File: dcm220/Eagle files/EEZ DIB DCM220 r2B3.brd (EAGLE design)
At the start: 145 x 95 mm, 231 parts, among them IC1 Si8662AB-B-IS1, IC10 LT3763EFE#PBF, IC11 MC33274ADR2G, IC12 LT3763EFE#PBF, IC2 TPS54060DGQ, IC3 Si8641AB-B-IS1, IC4 M24C32-WMN6P, IC5 LP2985-33DBVR, IC6 TPD4E001DRLR, IC7 MAX5715BAUD+, IC8 STM32F373C8T6, IC9 MC33272ADR2G, J1 4907, J2 571-0500, J3 571-0100, J4 571-0500, J5 571-0100, Q1 IRFR7546TRPBF, Q2 IRFR7546TRPBF, Q3 2N7002, Q4 BSS84, Q5 IRFR7546TRPBF, Q6 IRFR7546TRPBF, Q7 2N7002, Q8 BSS84, X1 172648-0102, X2 77317-104-28LF, X3 22-23-2061, X4 DS1024-2*5R0, Y1 LF XTAL026392

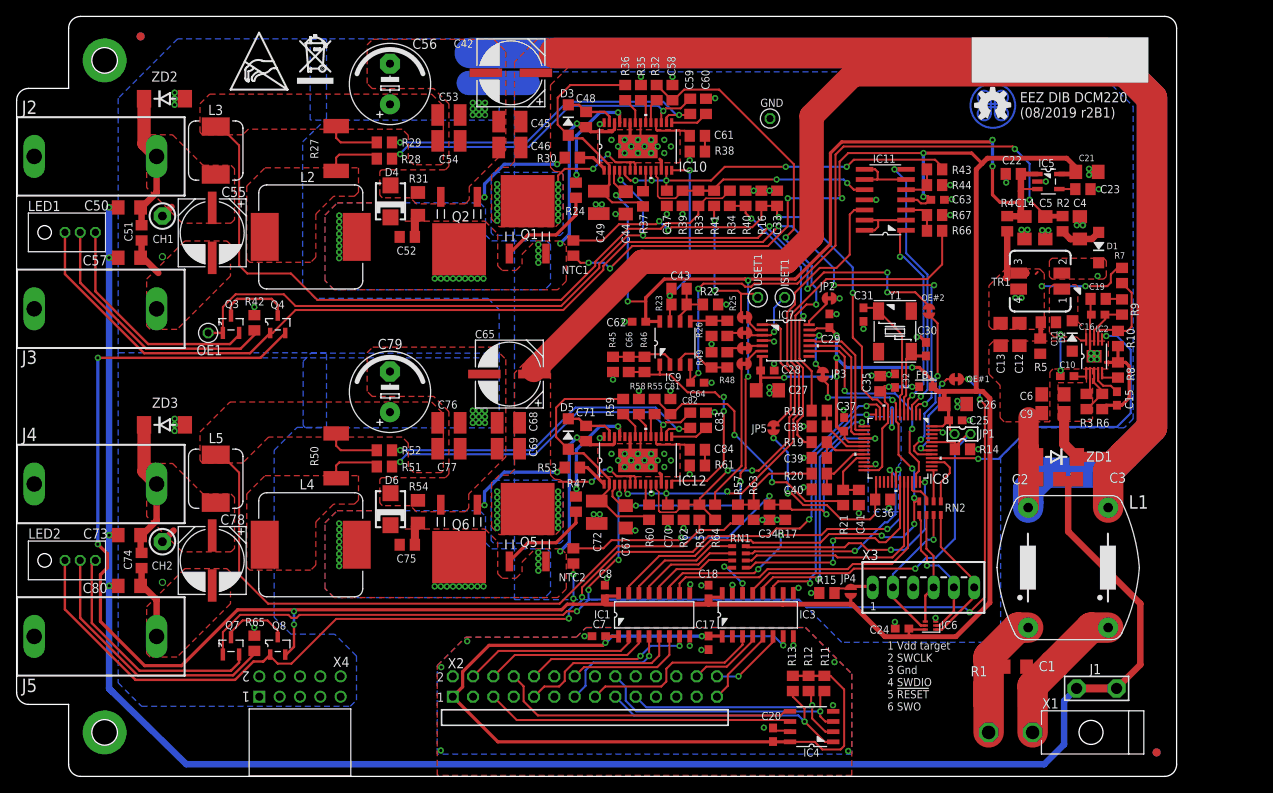
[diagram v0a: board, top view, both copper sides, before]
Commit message: #48, replaced DAC with PWM
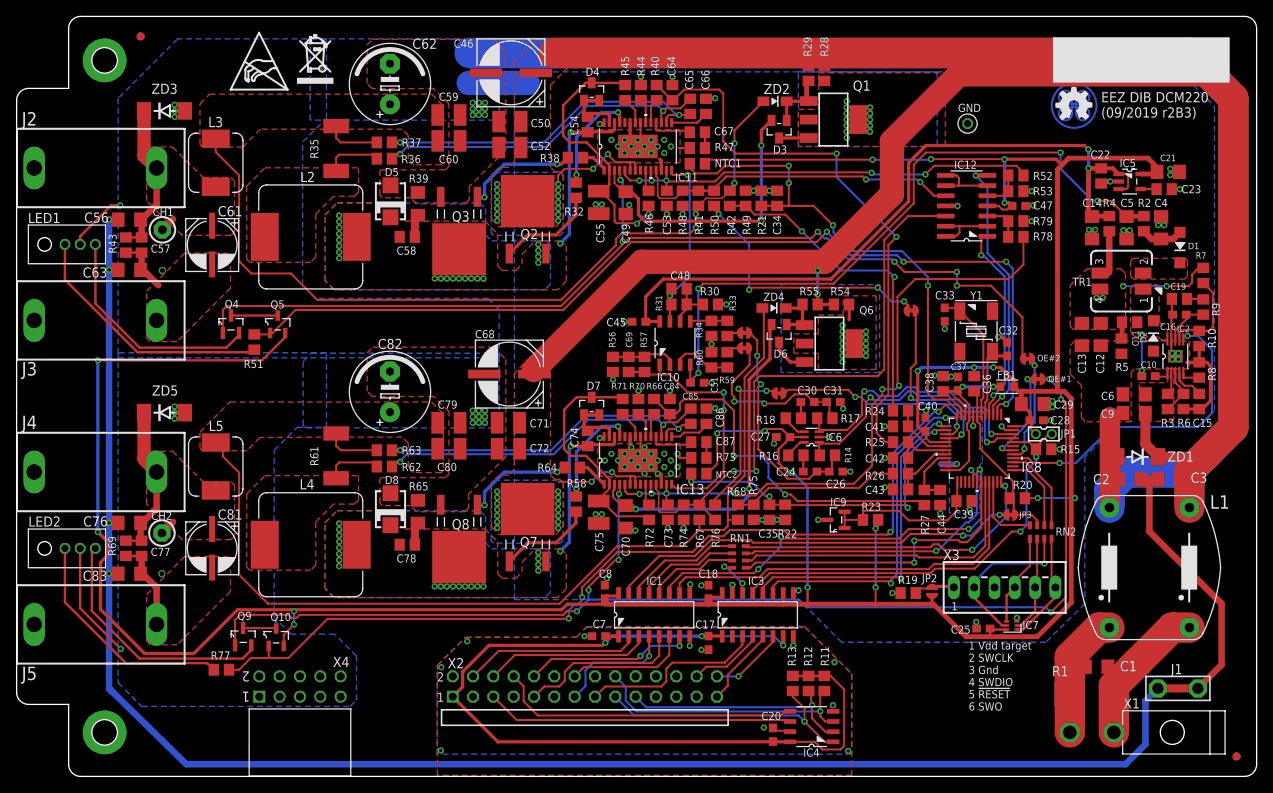
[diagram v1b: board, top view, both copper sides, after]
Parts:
- removed ISET1, OE1, USET1: (no value), EEZ_connectors:TEST-PIN_0.9MM
- removed JP4: JP2-CUT, EEZ_Lib1:JP2-CUT
- removed JP5: JP2-NOCUT, EEZ_Lib1:JP2-NOCUT
- added C85: 33n, rcl:C0805
- added C86: 10n, rcl:C0805
- added C87: 4n7, rcl:C0805
- added D7: BAW56L, EEZ_Lib1:SOT23
- added D8: N.C., EEZ_Lib1:SMA
- added IC13: LT3763EFE#PBF, EEZ_Lib1:LTC_05-08-1663-EB
- added Q10: BSS84, EEZ_Lib1:SOT95P237X112-3N
- added Q9: BSS205NH6327XTSA1, EEZ_Lib1:SOT103P240X110-3N
- added R68, R70: 86K6, rcl:R0805
- added R69: 3K3, rcl:R0805
- added R71, R72: 47K, rcl:R0805
- added R73: 30K, rcl:R0805
- added R74: 3K9, rcl:R0805
- added R75: 12K, rcl:R0805
- added R76: 3K6, rcl:R0805
- added R77: 120R, rcl:R0805
- added R78: 11K8, rcl:R0805
- added R79: 15K, rcl:R0805
- added ZD4: MM3Z9V1T1G, EEZ_Lib1:SOD323-W
- added ZD5: SMAJ51A, EEZ_Lib1:DO214AA
- C1, C2, C3: value 4n7/100V -> 10n/200V
- C15: value 100n -> 10n; device rcl:C0603 -> rcl:C0805
- C25: value 100n -> N.C.
- C26, C27: value 4u7 -> 100n; device rcl:C1206 -> rcl:C0603
- C29: value 100n -> 4u7; device rcl:C0603 -> rcl:C1206
- C30, C31: value 18p -> 100n
- C32: value 100n -> 4p7
- C33: value 10n -> 4p7; device rcl:C0805 -> rcl:C0603
- C35: value 1u -> 10n
- C36: value 100p -> 1n
- C38: value 3n3 -> 1u
- C39, C41: value 3n3 -> 4n7
- C40: value 3n3 -> 100n; device rcl:C0805 -> rcl:C0603
- C42: value EEEFK1V470P -> 4n7; device EEZ_Lib1:CAPAE830X1050N -> rcl:C0805
- C43: value 100p -> 4n7
- C44, C67: value 4u7 -> 4n7; device rcl:C1206 -> rcl:C0805
- C45: value 10u -> 100n; device rcl:C1210 -> rcl:C0603
- C46, C68: value 10u -> EEEFK1H470; device rcl:C1210 -> EEZ_Lib1:CAPAE830X1050N
- C47, C51: value 1u -> 100n; device rcl:C0805 -> rcl:C0603
- C48: value 220n -> 100p
- C49: value 22u -> 4u7; device rcl:C1210 -> rcl:C1206
- C50: value 10n/200V -> 10u; device rcl:C1206 -> rcl:C1210
- C52: value N.C. -> 10u; device rcl:C0805 -> rcl:C1210
- C53, C77: value 22u -> 1u; device rcl:C1210 -> rcl:C0805
- C54: value 22u -> 220n; device rcl:C1210 -> rcl:C0805
- C55: value EEEFK1V470P -> 22u; device EEZ_Lib1:CAPAE830X1050N -> rcl:C1210
- C56: value UVZ1E102MPD -> 10n/200V; device EEZ_Lib1:ECAP5/10.5 -> rcl:C1206
- C57, C73: value 10n/200V -> 1u; device rcl:C1206 -> rcl:C0805
- C58: value 470p -> N.C.
- C59: value 33n -> 22u; device rcl:C0805 -> rcl:C1210
- C60: value 10n -> 22u; device rcl:C0805 -> rcl:C1210
- C61: value 4n7 -> EEEFK1V470P; device rcl:C0805 -> EEZ_Lib1:CAPAE660X610N
- C62: value 100n -> UVZ1E102MPD; device rcl:C0603 -> EEZ_Lib1:ECAP5/10.5
- C63: value 100n -> 10n/200V; device rcl:C0603 -> rcl:C1206
- C64: value 100n -> 470p; device rcl:C0603 -> rcl:C0805
- C65: value EEEFK1V470P -> 33n; device EEZ_Lib1:CAPAE830X1050N -> rcl:C0805
- C66: value 100p -> 10n
- C69: value 10u -> 100p; device rcl:C1210 -> rcl:C0805
- C70: value 1u -> 4u7; device rcl:C0805 -> rcl:C1206
- C71: value 220n -> 10u; device rcl:C0805 -> rcl:C1210
- C72: value 22u -> 10u
- C74: value 1u -> 220n
- C75: value N.C. -> 22u; device rcl:C0805 -> rcl:C1210
- C76: value 22u -> 10n/200V; device rcl:C1210 -> rcl:C1206
- C78: value EEEFK1V470P -> N.C.; device EEZ_Lib1:CAPAE830X1050N -> rcl:C0805
- C79: value UVZ1E102MPD -> 22u; device EEZ_Lib1:ECAP5/10.5 -> rcl:C1210
- C80: value 10n/200V -> 22u; device rcl:C1206 -> rcl:C1210
- C81: value 470p -> EEEFK1V470P; device rcl:C0805 -> EEZ_Lib1:CAPAE660X610N
- C82: value 33n -> UVZ1E102MPD; device rcl:C0805 -> EEZ_Lib1:ECAP5/10.5
- C83: value 10n -> 10n/200V; device rcl:C0805 -> rcl:C1206
- C84: value 4n7 -> 470p
- D3: value SKL16 -> BAW56L; device EEZ_Lib1:SOD123 -> EEZ_Lib1:SOT23
- D4, D6: value N.C. -> BAW56L; device EEZ_Lib1:SMA -> EEZ_Lib1:SOT23
- D5: value SKL16 -> N.C.; device EEZ_Lib1:SOD123 -> EEZ_Lib1:SMA
- IC10: value LT3763EFE#PBF -> MC33272ADR2G; device EEZ_Lib1:LTC_05-08-1663-EB -> EEZ_Lib1:SOIC127P600X173-8N
- IC11: value MC33274ADR2G -> LT3763EFE#PBF; device EEZ_Lib1:SOIC127P600X175-14N -> EEZ_Lib1:LTC_05-08-1663-EB
- IC12: value LT3763EFE#PBF -> MC33274ADR2G; device EEZ_Lib1:LTC_05-08-1663-EB -> EEZ_Lib1:SOIC127P600X175-14N
- IC6: value TPD4E001DRLR -> 74HC2G04GW,125; device EEZ_Lib1:DRL6 -> EEZ_Lib1:SOT65P210X110-6N
- IC7: value MAX5715BAUD+ -> N.C.; device EEZ_Lib1:21-0066J_14 -> EEZ_Lib1:DRL6
- IC9: value MC33272ADR2G -> TL431B; device EEZ_Lib1:SOIC127P600X173-8N -> EEZ_Lib1:SOT103P240X110-3N
- JP2: value JP2-NOCUT -> JP2-CUT; device EEZ_Lib1:JP2-NOCUT -> EEZ_Lib1:JP2-CUT
- Q1, Q6: value IRFR7546TRPBF -> BSP716NH6327XTSA1; device EEZ_Lib1:TO229P990X239-3N -> transistor-power:SOT223
- Q2: value IRFR7546TRPBF -> NTD5867NLT4G
- Q3, Q7: value 2N7002 -> NTD5867NLT4G; device EEZ_Lib1:SOT103P240X110-3N -> EEZ_Lib1:TO229P990X239-3N
- Q4: value BSS84 -> BSS205NH6327XTSA1; device EEZ_Lib1:SOT95P237X112-3N -> EEZ_Lib1:SOT103P240X110-3N
- Q5: value IRFR7546TRPBF -> BSS84; device EEZ_Lib1:TO229P990X239-3N -> EEZ_Lib1:SOT95P237X112-3N
- Q8: value BSS84 -> NTD5867NLT4G; device EEZ_Lib1:SOT95P237X112-3N -> EEZ_Lib1:TO229P990X239-3N
- R1: value 4K7/2W -> N.C.
- R16, R17: value 3K3 -> 10K
- R18, R20: value 1K -> 10K
- R19: value 1K -> N.C.
- R21: value 1K -> 3K3
- R22: value 20K -> 3K3
- R23: value 12K -> 120R
- R24: value 0R -> 2K2
- R25: value 20K -> 2K2
- R26, R40: value 12K -> 2K2
- R27: value R012/2W -> 2K2; device EEZ_Lib1:R_2512-4WIRE -> rcl:R0805
- R29: value 10R -> 330K
- R30: value 0R -> 20K
- R31: value N.C. -> 12K; device rcl:R1206 -> rcl:R0805
- R32: value 2K2 -> 0R
- R33, R56: value 30K -> 20K
- R34, R57: value 86K6 -> 12K
- R35: value 86K6 -> R012/2W; device rcl:R0805 -> EEZ_Lib1:R_2512-4WIRE
- R36, R37: value 47K -> 10R
- R38: value 30K -> 0R
- R39: value 3K9 -> N.C.; device rcl:R0805 -> rcl:R1206
- R41: value 3K6 -> 30K
- R42: value 120R -> 86K6
- R43: value 11K8 -> 3K3
- R44: value 15K -> 86K6
- R45: value 20K -> 47K
- R46: value 12K -> 47K
- R47: value 0R -> 30K
- R48: value 20K -> 3K9
- R50: value R012/2W -> 3K6; device EEZ_Lib1:R_2512-4WIRE -> rcl:R0805
- R51: value 10R -> 120R
- R52: value 10R -> 11K8
- R53: value 0R -> 15K
- R54: value N.C. -> 10R; device rcl:R1206 -> rcl:R0805
- R55: value 2K2 -> 330K
- R58: value 86K6 -> 0R
- R59: value 47K -> 20K
- R60: value 47K -> 12K
- R61: value 30K -> R012/2W; device rcl:R0805 -> EEZ_Lib1:R_2512-4WIRE
- R62: value 3K9 -> 10R
- R63: value 12K -> 10R
- R64: value 3K6 -> 0R
- R65: value 120R -> N.C.; device rcl:R0805 -> rcl:R1206
- R66: value 11K8 -> 2K2
- R67: value 15K -> 30K
- RN2: value DR1206-33R-4/8 -> N.C.
- X3: value 22-23-2061 -> N.C.
- ZD2: value SMAJ51A -> MM3Z9V1T1G; device EEZ_Lib1:DO214AA -> EEZ_Lib1:SOD323-W
- moved R43 101.5 mm to (13.7, 66.4), turned to 270 degrees
- moved C63 101.4 mm to (14.1, 63.3)
- moved R52 86.1 mm to (124.9, 75.1), turned to 0 degrees
- moved R27 85.5 mm to (113.5, 34.9), turned to 270 degrees
- moved ZD2 76.3 mm to (94.8, 84.4), turned to 180 degrees
- moved C83 74.6 mm to (14.1, 25.3), turned to 0 degrees
- moved C51 72.0 mm to (85.1, 49.2), turned to 180 degrees
- moved C42 68.5 mm to (110.5, 39.8), turned to 0 degrees
- moved C73 67.4 mm to (81.4, 33.0), turned to 270 degrees
- moved R53 65.3 mm to (124.9, 73.2)
- moved C61 62.2 mm to (24.4, 66.4), turned to 270 degrees
- moved R42 61.4 mm to (89.2, 72.3)
- moved C81 60.0 mm to (24.4, 28.5)
- moved R54 59.0 mm to (103.1, 59.0), turned to 0 degrees
- moved C74 57.8 mm to (71.4, 42.2)
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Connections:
- removed net !DAC_CLR: IC7.12, JP3.1
- removed net !LDAC: IC7.14, JP2.1
- removed net DAC_MOSI: IC7.9, IC8.35
- removed net DAC_NSS: IC7.11, IC8.14
- removed net DAC_SCLK: IC7.10, IC8.15
- removed net N$266: IC7.3, ISET1.1, I_SET1.2
- removed net N$277: C66.1, IC12.14, IC9.1, R46.2
- removed net N$35: LED2.CC, R65.1
- removed net N$477: IC7.5, I_SET2.2
- removed net N$479: IC7.6, U_SET2.2
- removed net N$52: C36.2, IC8.25, JP5.1
- removed net REF_12: IC7.1, JP5.2
- new net +VREF: C39.2, IC8.25, IC9.1, IC9.2, R23.2
- new net ISET1: C48.1, IC10.7, IC11.14, R31.2
- new net ISET2: C69.1, IC10.1, IC13.14, R57.2
- new net I_SET_OUT#1: IC6.1, IC8.45, R14.2
- new net I_SET_OUT#2: IC6.3, IC8.46, R17.2
- new net N$246: C24.2, R16.1
- new net N$247: C24.1, C26.1, I_SET1.2, R14.1
- new net N$25: LED2.RED, R77.1
- new net N$26: D3.1, Q1.1, R29.2, ZD2.C
- new net N$39: C49.1, D3.2, IC11.3
- new net N$40: C30.2, R18.1
- new net N$42: C70.1, D6.2, IC13.3
- new net N$43: D3.3, Q1.3
- new net N$44: C30.1, C31.1, I_SET2.2, R17.1
- new net N$46: D6.1, Q6.1, R55.2, ZD4.C
- new net N$61: D6.3, Q6.3
- new net NRST: C36.1, IC8.7, JP3.2, R20.2, RN2.3
- new net Q1D: Q1.2, Q1.4, R28.2
- new net Q6D: Q6.2, Q6.4, R54.2
- new net U_SET_OUT#1: IC8.16, U_SET1.2
- new net U_SET_OUT#2: IC8.15, U_SET2.2
- net !RESET: now also JP3.1; no longer IC8.7, JP3.2, RN2.4
- net +3V3: now also C25.1, C29.1, C36.2, C40.2, C47.1, IC12.4, IC6.5, IC7.6, JP2.1, Q10.2, Q5.2, R20.1, R23.1; no longer C24.1, C25.2, C26.1, C29.2, C37.2, C63.1, IC11.4, IC6.6, IC7.13, IC7.7, JP4.1, Q4.2, Q8.2
- net +8V: now also C45.1, IC10.8; no longer C44.1, C62.1, C67.1, IC10.3, IC12.3, IC9.8
- net -8V: now also C51.2, IC10.4; no longer C64.2, IC9.4
- net AGND: now also C39.1; no longer C36.1
- net BOOT0: now also R15.2; no longer R14.2
- net CC#1: now also IC12.7; no longer IC11.7
- net CC#2: now also IC12.1; no longer IC11.1
- net CC_LED#1: now also Q5.1, R51.2; no longer LED1.RED, Q4.1
- net CC_LED#2: now also Q10.1, R77.2; no longer LED2.RED, Q8.1
- net DC_OUT+: now also C46.+, C50.1, C52.1, C68.+, C71.1, C72.1, IC11.6, IC11.7, IC13.6, IC13.7, Q2.2, Q7.2, R28.1, R29.1, R54.1, R55.1; no longer C42.+, C45.1, C46.1, C65.+, C68.1, C69.1, IC10.6, IC10.7, IC12.6, IC12.7, Q1.2, Q5.2
- net DC_OUT-: now also C46.-, C50.2, C52.2, C59.2, C60.2, C61.2, C62.-, C63.2, C68.-, C71.2, C72.2, C79.2, C81.2, C82.-, C83.2, D5.A, D8.A, LED1.CC, LED2.CC, Q3.3, Q8.3, R39.1, R43.2, R65.1, R69.2, ZD5.A; no longer C42.-, C45.2, C46.2, C51.2, C53.2, C54.2, C55.-, C56.-, C65.-, C68.2, C69.2, C74.2, C76.2, C78.-, C79.-, D4.A, D6.A, Q2.3, Q6.3, R31.1, R42.2, R54.1, R65.2, ZD2.A
- net FB1: now also IC11.11, IC12.10, R41.1, R48.2, R50.2; no longer IC10.11, IC11.10, R33.1, R39.2, R41.2
- net FB2: now also IC12.12, IC13.11, R67.1, R74.2, R76.2; no longer IC11.12, IC12.11, R56.1, R62.2, R64.2
- net GND: now also C25.2, C29.2, C31.2, C42.1, C43.1, C44.1, C45.2, C51.1, C53.2, C55.2, C66.1, C73.2, C75.2, C84.1, C86.1, IC11.12, IC11.21, IC11.23, IC11.28, IC11.TP, IC12.11, IC13.12, IC13.21, IC13.23, IC13.28, IC13.TP, IC6.2, IC7.3, IC9.3, R19.1, R21.2, R22.2, R30.1, R34.1, R47.1, R48.1, R53.1, R56.1, R60.1, R70.1, R73.1, R74.1, R75.1, R79.1; no longer C24.2, C25.1, C29.1, C30.1, C31.1, C39.1, C44.2, C58.1, C60.1, C62.2, C63.2, C67.2, C72.2, C81.1, C83.1, IC10.12, IC10.21, IC10.23, IC10.28, IC10.TP, IC11.11, IC12.12, IC12.21, IC12.23, IC12.28, IC12.TP, IC6.3, IC7.4, JP2.2, R14.1, R16.2, R17.2, R22.1, R26.1, R35.1, R38.1, R39.1, R40.1, R45.1, R58.1, R61.1, R62.1, R63.1, R67.1
- net INTVCC1: now also C55.1, D4.3, IC11.2, R45.1, R46.2; no longer C49.1, D3.A, IC10.2, R36.1, R37.2
- net INTVCC2: now also C75.1, D7.3, IC13.2, R71.1, R72.2; no longer C72.1, D5.A, IC12.2, R59.1, R60.2
- net I_MON#1: now also C42.2, R25.1; no longer C39.2, R19.1
- net I_MON#2: now also C44.2, R27.1; no longer C41.2, R21.1
- net I_MON1: now also C64.2, R25.2, R40.1; no longer C58.2, R19.2, R32.1
- net I_MON2: now also C84.2, R27.2, R66.1; no longer C81.2, R21.2, R55.1
- net I_SET#1: now also R33.1; no longer R25.1
- net I_SET#2: now also R59.1; no longer R48.1
- net LOUT1: now also R35.1; no longer R27.1
- net LOUT2: now also R61.1; no longer R50.1
- net N$1: now also IC11.1, R38.1; no longer IC10.1, R30.1
- net N$11: now also LED1.RED, R51.1; no longer LED1.CC, R42.1
- net N$12: now also C66.2, IC11.15; no longer C60.2, IC10.15
- net N$13: now also C67.1, R47.2; no longer C61.1, R38.2
- net N$14: now also C67.2, IC11.18; no longer C61.2, IC10.18
- net N$15: now also IC11.25, R32.1; no longer IC10.25, R24.1
- net N$16: now also R35.2S, R37.2; no longer R27.2S, R29.2
- net N$17: now also C58.2, R39.2; no longer C52.2, R31.2
- net N$18: now also IC11.9, R46.1; no longer IC10.9, R37.1
- net N$19: now also Q2.1, R32.2; no longer Q1.1, R24.2
- net N$2: now also Q3.1, R38.2; no longer Q2.1, R30.2
- net N$22: now also C54.1, D4.1, D4.2, IC11.27; no longer C48.1, D3.C, IC10.27
- net N$249: now also C87.2, IC13.18; no longer C84.2, IC12.18
- net N$250: now also IC10.5, R33.2, R34.2; no longer IC9.5, R25.2, R26.2
- net N$251: now also C48.2, IC10.6, R30.2, R31.1; no longer C43.2, IC9.6, R22.2, R23.1
- net N$252: now also IC6.6, R16.2; no longer C43.1, IC10.14, IC9.7, R23.2
- net N$253: now also IC13.9, R72.1; no longer IC12.9, R60.1
- net N$255: now also IC13.25, R58.1; no longer IC12.25, R47.1
- net N$256: now also Q7.1, R58.2; no longer Q5.1, R47.2
- net N$257: now also IC13.1, R64.1; no longer IC12.1, R53.1
- net N$258: now also Q8.1, R64.2; no longer Q6.1, R53.2
- net N$261: now also R61.1S, R62.2; no longer R50.1S, R51.2
- net N$262: now also R61.2S, R63.2; no longer R50.2S, R52.2
- net N$263: now also C78.2, R65.2; no longer C75.2, R54.2
- net N$264: now also C74.1, D7.1, D7.2, IC13.27; no longer C71.1, D5.C, IC12.27
- net N$267: now also IC13.19, R66.2; no longer IC12.19, R55.2
- net N$27: now also Q4.2; no longer Q3.2
- net N$270: now also IC12.13, IC12.14, IC12.2; no longer IC11.13, IC11.14, IC11.2
- net N$271: now also IC12.3, R78.1, R79.2; no longer IC11.3, R66.1, R67.2
- net N$278: now also C69.2, IC10.2, R56.2, R57.1; no longer C66.2, IC9.2, R45.2, R46.1
- net N$28: now also IC13.20, R70.2; no longer IC12.20, R58.2
- net N$3: now also Q5.3; no longer Q3.3
- net N$311: now also IC10.3, R59.2, R60.2; no longer IC9.3, R48.2, R49.2
- net N$36: now also C86.2, IC13.15; no longer C83.2, IC12.15
- net N$37: now also C87.1, R73.2; no longer C84.1, R61.2
- net N$38: now also Q10.3, Q9.3; no longer Q7.3, Q8.3
- net N$41: now also Q9.2; no longer Q7.2
- net N$45: now also IC6.4, R18.2; no longer IC7.2, U_SET1.2
- net N$48: now also IC11.19, R40.2; no longer IC10.19, R32.2
- net N$49: now also IC7.1; no longer IC6.1
- net N$50: now also IC7.2, RN2.6; no longer IC6.2, RN2.5
- net N$51: now also JP2.2, R19.2; no longer JP4.2, R15.2
- net N$54: now also IC12.5, R52.1, R53.2; no longer IC11.5, R43.1, R44.2
- net N$55: now also IC12.6, IC12.8, IC12.9; no longer IC11.6, IC11.8, IC11.9
- net N$7: now also R35.1S, R36.2; no longer R27.1S, R28.2
- net N$8: now also IC11.20, R44.2; no longer IC10.20, R35.2
- net OE#1: now also IC11.4, Q4.1; no longer IC10.4, OE1.1, Q3.1
- net OE#2: now also IC13.4, Q9.1; no longer IC12.4, Q7.1
- net PE: now also C56.1, C63.1, C76.1, C83.1; no longer C50.1, C57.1, C73.1, C80.1
- net PWM#1: now also IC11.22, R45.2; no longer IC10.22, R36.2
- net PWM#2: now also IC13.22, R71.2; no longer IC12.22, R59.2
- net RCC_OSC_IN: now also C32.2; no longer C30.2
- net RCC_OSC_OUT: now also C33.2; no longer C31.2
- net SENSE1+: now also C65.1, IC11.17, R36.1; no longer C59.1, IC10.17, R28.1
- net SENSE1+1: now also C85.1, IC13.17, R62.1; no longer C82.1, IC12.17, R51.1
- net SENSE1-: now also C65.2, IC11.16, R37.1; no longer C59.2, IC10.16, R29.1
- net SENSE1-1: now also C85.2, IC13.16, R63.1; no longer C82.2, IC12.16, R52.1
- net SW1: now also C54.2, C58.1, D5.C, IC11.26, Q2.3, Q3.2; no longer C48.2, C52.1, D4.C, IC10.26, Q1.3, Q2.2
- net SW2: now also C74.2, C78.1, D8.C, IC13.26, Q7.3, Q8.2; no longer C71.2, C75.1, D6.C, IC12.26, Q5.3, Q6.2
- net SWDIO: now also RN2.4; no longer RN2.3
- net TCK: now also IC7.5; no longer IC6.5
- net TEMP#1: now also C34.2, R21.1; no longer C33.2, R16.1
- net TEMP#2: now also C35.2, IC8.14, R22.1; no longer C34.2, IC8.16, R17.1
- net TMS: now also IC7.4, RN2.5; no longer IC6.4, RN2.6
- net U_MON#1: now also C41.2, R24.1; no longer C38.2, R18.1
- net U_MON#2: now also C43.2, R26.1; no longer C40.2, R20.1
- net U_MON1: now also R24.2, R42.1, R49.2; no longer R18.2, R34.1, R40.2
- net U_MON2: now also R26.2, R68.1, R75.2; no longer R20.2, R57.1, R63.2
- net U_SET#1: now also R50.1; no longer R41.1, USET1.1
- net U_SET#2: now also R76.1; no longer R64.1
- net VDDA: now also C37.2, C38.2; no longer C32.2, C35.2
- net VOUT1+: now also C59.1, C60.1, C62.+, R35.2, R41.2, R42.2, ZD2.A; no longer C53.1, C54.1, C56.+, R27.2, R33.2, R34.2
- net VOUT2+: now also C79.1, C80.1, C82.+, R61.2, R67.2, R68.2, ZD4.A; no longer C76.1, C77.1, C79.+, R50.2, R56.2, R57.2
- net VOUT_LC1+: now also C56.2, C57.1, C61.1, R43.1, ZD3.C; no longer C50.2, C51.1, C55.+, ZD2.C
- net VOUT_LC2+: now also C76.2, C77.1, C81.1, R69.1, ZD5.C; no longer C73.2, C74.1, C78.+, ZD3.C
- net VREF1: now also C53.1, IC11.10, IC11.13, IC11.5, R52.2; no longer C47.1, IC10.10, IC10.13, IC10.5, R43.2
- net VREF2: now also C73.1, IC13.10, IC13.13, IC13.5, R78.2; no longer C70.1, IC12.10, IC12.13, IC12.5, R66.2
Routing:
- net +8V: track 153.6 -> 89.9 mm, vias 8 -> 2
- net N$42: track 0.00 -> 42.7 mm, vias 0 -> 2
- net N$39: track 0.00 -> 36.2 mm, vias 0 -> 2
- net DC_OUT-: track 188.1 -> 223.7 mm
- net I_SET_OUT#1: track 0.00 -> 34.8 mm, vias 0 -> 2
- net I_SET_OUT#2: track 0.00 -> 34.4 mm, vias 0 -> 2
- net N$35: track 33.4 -> 0.00 mm
- net ISET2: track 0.00 -> 32.5 mm, vias 0 -> 2
- net N$277: track 30.9 -> 0.00 mm, vias 2 -> 0
- net VOUT2+: track 86.3 -> 116.5 mm
- net N$25: track 0.00 -> 28.8 mm
- net N$247: track 0.00 -> 28.5 mm, vias 0 -> 2
- net DAC_MOSI: track 28.1 -> 0.00 mm, vias 2 -> 0
- net DC_OUT+: track 271.9 -> 298.6 mm, vias 32 -> 34
- net U_SET_OUT#2: track 0.00 -> 26.6 mm, vias 0 -> 2
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- added copper zone on layer 1, net Q1D
- added copper zone on layer 16, net Q1D
- added copper zone on layer 1, net Q6D
- added copper zone on layer 16, net Q6D
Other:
- board size 145 x 95 mm -> 155 x 95 mm
- board text added: "EEZ DIB DCM220 (09/2019 r2B3)"
- board text added: "EEZ DIB DCM220 (09/2019 r2B3) Project source code: github.com/eez-open"
- board text removed: "EEZ DIB DCM220 (08/2019 r2B1)"
- board text removed: "EEZ DIB DCM220 (08/2019 r2B1) Project source code: github.com/eez-open"

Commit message: DCM220 I_SET gain adjustment
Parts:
- R30, R33, R56, R59: value 20K -> 22K
- R31, R34, R57, R60: value 12K -> 10K
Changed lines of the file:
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@@
 <attribute name="VALUE" x="77.7081" y="53.894" size="0.8128" layer="27" ratio="10" rot="SR0"/>
 </element>
-<element name="R31" library="rcl" package="R0805" value="12K" x="82.804" y="58.9915" smashed="yes" rot="R180">
+<element name="R31" library="rcl" package="R0805" value="10K" x="82.804" y="58.9915" smashed="yes" rot="R180">
 <attribute name="NAME" x="79.883" y="60.1345" size="0.8128" layer="25" ratio="10" rot="R270"/>
 <attribute name="VALUE" x="81.5975" y="58.42" size="1.016" layer="27" ratio="10"/>
 </element>
-<element name="R30" library="rcl" package="R0805" value="20K" x="86.741" y="58.9915" smashed="yes" rot="R180">
+<element name="R30" library="rcl" package="R0805" value="22K" x="86.741" y="58.9915" smashed="yes" rot="R180">
 <attribute name="NAME" x="85.4075" y="60.1345" size="1.016" layer="25" ratio="10"/>
 <attribute name="VALUE" x="85.598" y="58.4835" size="1.016" layer="27" ratio="10"/>
@@
 <attribute name="VALUE" x="28.575" y="13.5001" size="0.6096" layer="27" ratio="10" rot="SR90"/>
 </element>
-<element name="R57" library="rcl" package="R0805" value="12K" x="78.486" y="51.4985" smashed="yes" rot="R270">
+<element name="R57" library="rcl" package="R0805" value="10K" x="78.486" y="51.4985" smashed="yes" rot="R270">
 <attribute name="NAME" x="78.8035" y="53.594" size="0.8128" layer="25" ratio="10" rot="R90"/>
 <attribute name="VALUE" x="78.994" y="50.2285" size="1.016" layer="27" ratio="10" rot="R90"/>
 </element>
-<element name="R56" library="rcl" package="R0805" value="20K" x="74.549" y="51.4985" smashed="yes" rot="R90">
+<element name="R56" library="rcl" package="R0805" value="22K" x="74.549" y="51.4985" smashed="yes" rot="R90">
 <attribute name="NAME" x="74.8665" y="53.594" size="0.8128" layer="25" ratio="10" rot="R90"/>
 <attribute name="VALUE" x="74.041" y="52.959" size="1.016" layer="27" ratio="10" rot="R270"/>
@@
 <attribute name="VALUE" x="36.7665" y="28.956" size="1.016" layer="27" ratio="10" rot="R180" align="center"/>
 </element>
-<element name="R34" library="rcl" package="R0805" value="12K" x="86.868" y="56.007" smashed="yes" rot="R90">
+<element name="R34" library="rcl" package="R0805" value="10K" x="86.868" y="56.007" smashed="yes" rot="R90">
 <attribute name="NAME" x="85.725" y="54.8005" size="0.8128" layer="25" ratio="10" rot="R90"/>
 <attribute name="VALUE" x="87.4395" y="54.864" size="1.016" layer="27" ratio="10" rot="R90"/>
 </element>
-<element name="R33" library="rcl" package="R0805" value="20K" x="88.8365" y="56.007" smashed="yes" rot="R90">
+<element name="R33" library="rcl" package="R0805" value="22K" x="88.8365" y="56.007" smashed="yes" rot="R90">
 <attribute name="NAME" x="89.916" y="58.166" size="0.8128" layer="25" ratio="10" rot="R90"/>
 <attribute name="VALUE" x="89.281" y="54.737" size="1.016" layer="27" ratio="10" rot="R90"/>
 </element>
-<element name="R60" library="rcl" package="R0805" value="12K" x="86.868" y="52.07" smashed="yes" rot="R270">
+<element name="R60" library="rcl" package="R0805" value="10K" x="86.868" y="52.07" smashed="yes" rot="R270">
 <attribute name="NAME" x="84.963" y="53.34" size="0.8128" layer="25" ratio="10" rot="R270"/>
 <attribute name="VALUE" x="87.249" y="50.8635" size="1.016" layer="27" ratio="10" rot="R90"/>
 </element>
-<element name="R59" library="rcl" package="R0805" value="20K" x="88.8365" y="52.07" smashed="yes" rot="R270">
+<element name="R59" library="rcl" package="R0805" value="22K" x="88.8365" y="52.07" smashed="yes" rot="R270">
 <attribute name="NAME" x="87.8205" y="49.149" size="0.8128" layer="25" ratio="10"/>
 <attribute name="VALUE" x="89.281" y="50.927" size="1.016" layer="27" ratio="10" rot="R90"/>
